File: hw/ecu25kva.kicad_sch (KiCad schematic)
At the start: 0 parts

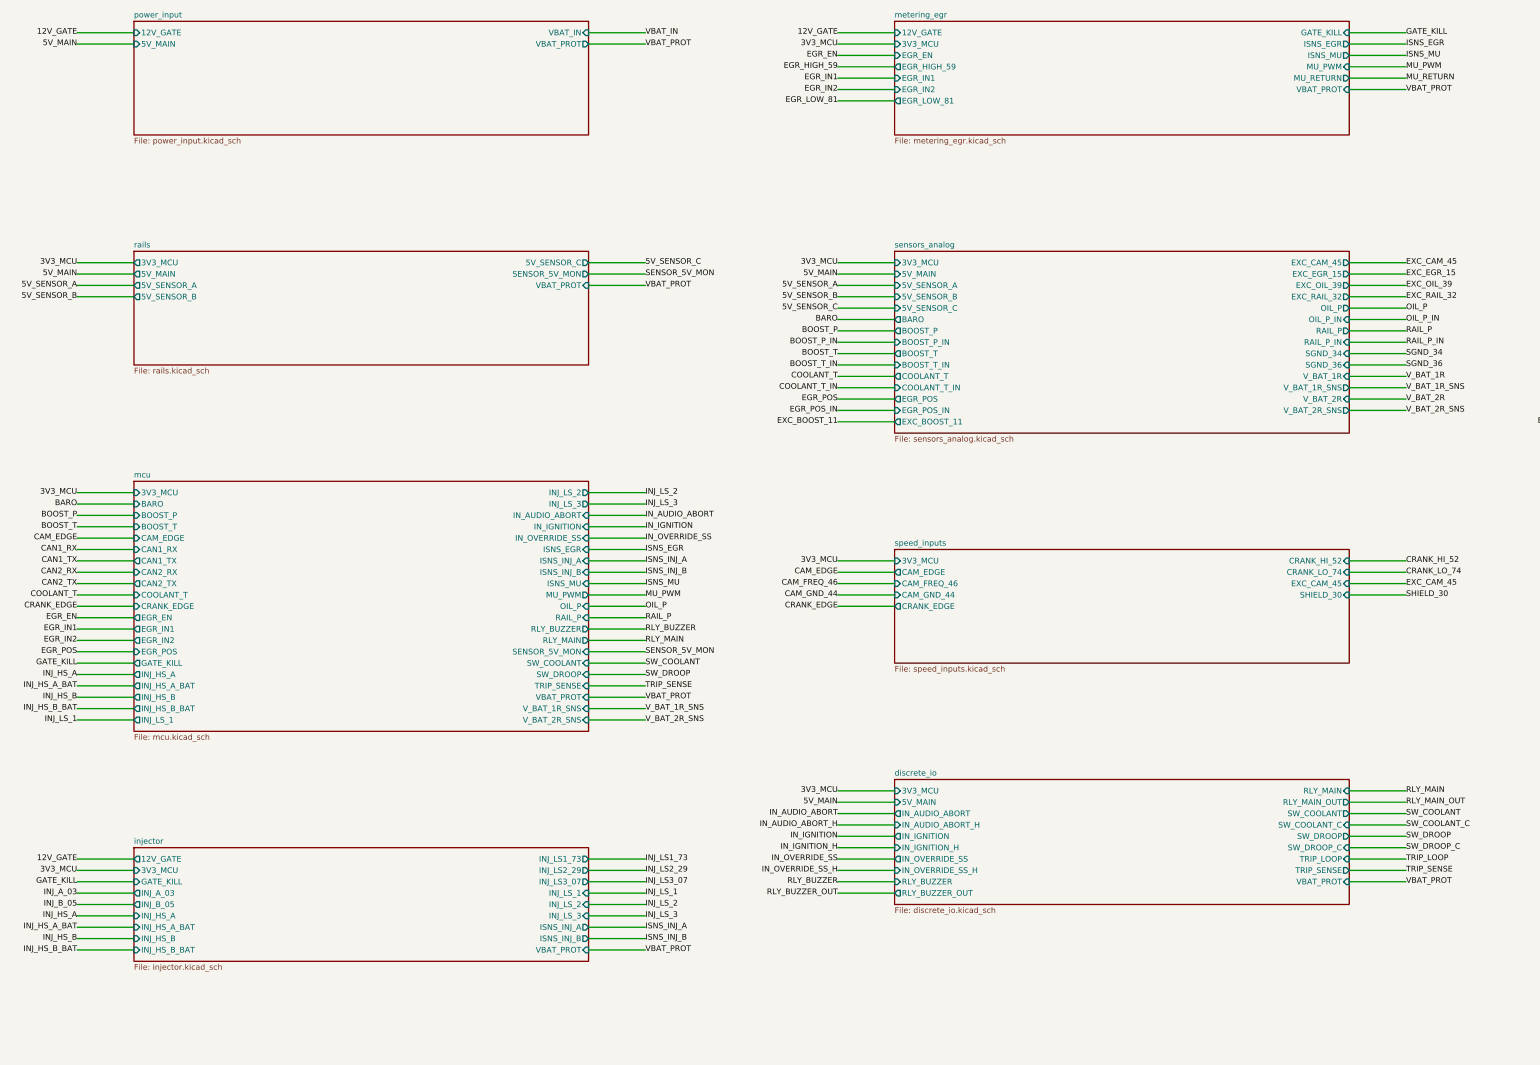
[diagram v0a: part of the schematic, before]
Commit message: Move the injector and EGR supply onto pins 04 and 06 (POWER-PATH)
Every high-current load drew through pin 21, whose reverse FET was
sized for 5 A and whose EMI filter never stated a DC current. Pin 04
now feeds VBAT_INJ (the injector hold switches and the boost power
stage), and pin 06 feeds VBAT_EGR (the EGR bridge). Each is fused 10 A
in the loom and has its own SMCJ43CA TVS, SQM120P10-10m1L reverse
P-FET (passive gate, as Q1), SS20PH102HM3 backstop and 2 x 2.2 uF.
Pin 21 keeps the buck, the relays, the metering freewheel and the
boost controller's VDD.

The pin-21 FET could not simply be copied: at the EGR's 6.4 A stall it
would pass its junction limit on a 105 C board. The new part, from
Vishay doc 76943 Rev. A, runs at Tj 139 C (155 C cranking) on the EGR
rail and 117 C on the injector rail. The new block power_path.cir
holds those figures as 18 checks. check_netlist now fails unless each
rail leaves its own FET for its own loads and VBAT_PROT reaches
neither power stage.

The sheets are generated against KiCad 7.0.11's symbol library, which
regenerates an unchanged sheet identically. KiCad 10's library would
have rewritten every embedded symbol.

Gates: 25/25 blocks; connectivity OK with the same 2 open items; 333
components, 314 with footprints; 208 passives packaged. The questions
put to the owner -- the split, the reverse protection, what stays on
pin 21, and the KiCad/ngspice choices -- are in decisions-log.md
sections 5 and 6. The spec, the BOM requirements, the handbook, status
and the handoff are updated to match, and the bible is rebuilt (333
pages).
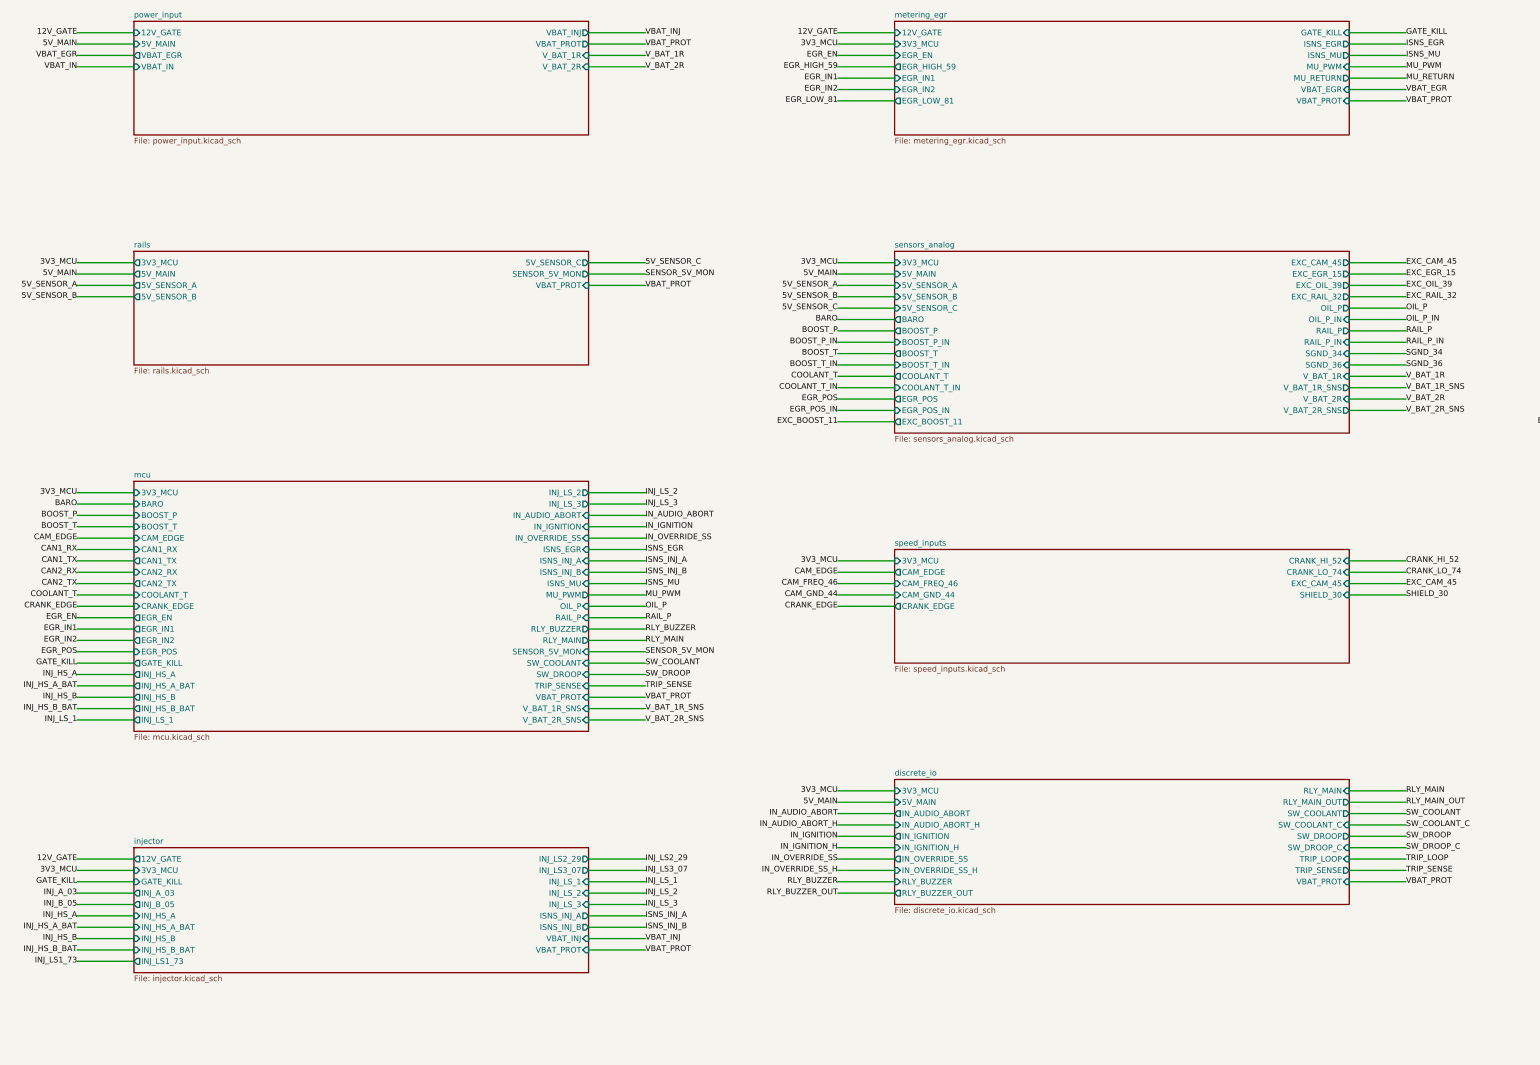
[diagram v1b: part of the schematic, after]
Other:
- sheet injector ports: added VBAT_INJ; removed none
- sheet metering_egr ports: added VBAT_EGR; removed none
- sheet power_input ports: added VBAT_EGR, VBAT_INJ, V_BAT_1R, V_BAT_2R; removed none
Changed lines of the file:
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@@
       (effects (font (size 1.27 1.27)) (justify left))
     )
-    (pin "VBAT_IN" input (at 146.60 30.54 0)
+    (pin "VBAT_EGR" output (at 45.00 35.62 180)
+      (effects (font (size 1.27 1.27)) (justify left))
+    )
+    (pin "VBAT_IN" input (at 45.00 38.16 180)
+      (effects (font (size 1.27 1.27)) (justify left))
+    )
+    (pin "VBAT_INJ" output (at 146.60 30.54 0)
       (effects (font (size 1.27 1.27)) (justify right))
     )
     (pin "VBAT_PROT" output (at 146.60 33.08 0)
+      (effects (font (size 1.27 1.27)) (justify right))
+    )
+    (pin "V_BAT_1R" input (at 146.60 35.62 0)
+      (effects (font (size 1.27 1.27)) (justify right))
+    )
+    (pin "V_BAT_2R" input (at 146.60 38.16 0)
       (effects (font (size 1.27 1.27)) (justify right))
     )
@@
     )
   )
-  (sheet (at 45.0 212.68) (size 101.6 25.40) (fields_autoplaced)
+  (sheet (at 45.0 212.68) (size 101.6 27.94) (fields_autoplaced)
     (stroke (width 0.1524) (type solid))
     (fill (color 0 0 0 0.0000))
@@
       (effects (font (size 1.27 1.27)) (justify left bottom))
     )
-    (property "Sheetfile" "injector.kicad_sch" (id 1) (at 45.0 238.64 0)
+    (property "Sheetfile" "injector.kicad_sch" (id 1) (at 45.0 241.18 0)
       (effects (font (size 1.27 1.27)) (justify left top))
     )
@@
       (effects (font (size 1.27 1.27)) (justify left))
     )
-    (pin "INJ_LS1_73" output (at 146.60 215.22 0)
-      (effects (font (size 1.27 1.27)) (justify right))
-    )
-    (pin "INJ_LS2_29" output (at 146.60 217.76 0)
-      (effects (font (size 1.27 1.27)) (justify right))
-    )
-    (pin "INJ_LS3_07" output (at 146.60 220.30 0)
-      (effects (font (size 1.27 1.27)) (justify right))
-    )
-    (pin "INJ_LS_1" input (at 146.60 222.84 0)
-      (effects (font (size 1.27 1.27)) (justify right))
-    )
-    (pin "INJ_LS_2" input (at 146.60 225.38 0)
-      (effects (font (size 1.27 1.27)) (justify right))
-    )
-    (pin "INJ_LS_3" input (at 146.60 227.92 0)
-      (effects (font (size 1.27 1.27)) (justify right))
-    )
-    (pin "ISNS_INJ_A" output (at 146.60 230.46 0)
-      (effects (font (size 1.27 1.27)) (justify right))
-    )
-    (pin "ISNS_INJ_B" output (at 146.60 233.00 0)
+    (pin "INJ_LS1_73" output (at 45.00 238.08 180)
+      (effects (font (size 1.27 1.27)) (justify left))
+    )
+    (pin "INJ_LS2_29" output (at 146.60 215.22 0)
+      (effects (font (size 1.27 1.27)) (justify right))
+    )
+    (pin "INJ_LS3_07" output (at 146.60 217.76 0)
+      (effects (font (size 1.27 1.27)) (justify right))
+    )
+    (pin "INJ_LS_1" input (at 146.60 220.30 0)
+      (effects (font (size 1.27 1.27)) (justify right))
+    )
+    (pin "INJ_LS_2" input (at 146.60 222.84 0)
+      (effects (font (size 1.27 1.27)) (justify right))
+    )
+    (pin "INJ_LS_3" input (at 146.60 225.38 0)
+      (effects (font (size 1.27 1.27)) (justify right))
+    )
+    (pin "ISNS_INJ_A" output (at 146.60 227.92 0)
+      (effects (font (size 1.27 1.27)) (justify right))
+    )
+    (pin "ISNS_INJ_B" output (at 146.60 230.46 0)
+      (effects (font (size 1.27 1.27)) (justify right))
+    )
+    (pin "VBAT_INJ" input (at 146.60 233.00 0)
       (effects (font (size 1.27 1.27)) (justify right))
     )
@@
       (effects (font (size 1.27 1.27)) (justify right))
     )
-    (pin "VBAT_PROT" input (at 316.60 43.24 0)
+    (pin "VBAT_EGR" input (at 316.60 43.24 0)
+      (effects (font (size 1.27 1.27)) (justify right))
+    )
+    (pin "VBAT_PROT" input (at 316.60 45.78 0)
       (effects (font (size 1.27 1.27)) (justify right))
     )
@@
     (effects (font (size 1.27 1.27)) (justify right))
   )
+  (wire (pts (xy 45.00 35.62) (xy 32.30 35.62))
+    (stroke (width 0) (type default))
+  )
+  (label "VBAT_EGR" (at 32.30 35.62 180)
+    (effects (font (size 1.27 1.27)) (justify right))
+  )
+  (wire (pts (xy 45.00 38.16) (xy 32.30 38.16))
+    (stroke (width 0) (type default))
+  )
+  (label "VBAT_IN" (at 32.30 38.16 180)
+    (effects (font (size 1.27 1.27)) (justify right))
+  )
   (wire (pts (xy 146.60 30.54) (xy 159.30 30.54))
     (stroke (width 0) (type default))
   )
-  (label "VBAT_IN" (at 159.30 30.54 0)
+  (label "VBAT_INJ" (at 159.30 30.54 0)
     (effects (font (size 1.27 1.27)) (justify left))
   )
@@
     (effects (font (size 1.27 1.27)) (justify left))
   )
+  (wire (pts (xy 146.60 35.62) (xy 159.30 35.62))
+    (stroke (width 0) (type default))
+  )
+  (label "V_BAT_1R" (at 159.30 35.62 0)
+    (effects (font (size 1.27 1.27)) (justify left))
+  )
+  (wire (pts (xy 146.60 38.16) (xy 159.30 38.16))
+    (stroke (width 0) (type default))
+  )
+  (label "V_BAT_2R" (at 159.30 38.16 0)
+    (effects (font (size 1.27 1.27)) (justify left))
+  )
   (wire (pts (xy 45.00 81.94) (xy 32.30 81.94))
     (stroke (width 0) (type default))
@@
     (effects (font (size 1.27 1.27)) (justify right))
   )
+  (wire (pts (xy 45.00 238.08) (xy 32.30 238.08))
+    (stroke (width 0) (type default))
+  )
+  (label "INJ_LS1_73" (at 32.30 238.08 180)
+    (effects (font (size 1.27 1.27)) (justify right))
+  )
   (wire (pts (xy 146.60 215.22) (xy 159.30 215.22))
     (stroke (width 0) (type default))
   )
-  (label "INJ_LS1_73" (at 159.30 215.22 0)
+  (label "INJ_LS2_29" (at 159.30 215.22 0)
     (effects (font (size 1.27 1.27)) (justify left))
   )
@@
     (stroke (width 0) (type default))
   )
-  (label "INJ_LS2_29" (at 159.30 217.76 0)
+  (label "INJ_LS3_07" (at 159.30 217.76 0)
     (effects (font (size 1.27 1.27)) (justify left))
   )
@@
     (stroke (width 0) (type default))
   )
-  (label "INJ_LS3_07" (at 159.30 220.30 0)
+  (label "INJ_LS_1" (at 159.30 220.30 0)
     (effects (font (size 1.27 1.27)) (justify left))
   )
@@
     (stroke (width 0) (type default))
   )
-  (label "INJ_LS_1" (at 159.30 222.84 0)
+  (label "INJ_LS_2" (at 159.30 222.84 0)
     (effects (font (size 1.27 1.27)) (justify left))
   )
@@
     (stroke (width 0) (type default))
   )
-  (label "INJ_LS_2" (at 159.30 225.38 0)
+  (label "INJ_LS_3" (at 159.30 225.38 0)
     (effects (font (size 1.27 1.27)) (justify left))
   )
@@
     (stroke (width 0) (type default))
   )
-  (label "INJ_LS_3" (at 159.30 227.92 0)
+  (label "ISNS_INJ_A" (at 159.30 227.92 0)
     (effects (font (size 1.27 1.27)) (justify left))
   )
@@
     (stroke (width 0) (type default))
   )
-  (label "ISNS_INJ_A" (at 159.30 230.46 0)
+  (label "ISNS_INJ_B" (at 159.30 230.46 0)
     (effects (font (size 1.27 1.27)) (justify left))
   )
@@
     (stroke (width 0) (type default))
   )
-  (label "ISNS_INJ_B" (at 159.30 233.00 0)
+  (label "VBAT_INJ" (at 159.30 233.00 0)
     (effects (font (size 1.27 1.27)) (justify left))
   )
@@
     (stroke (width 0) (type default))
   )
-  (label "VBAT_PROT" (at 329.30 43.24 0)
-    (effects (font (size 1.27 1.27)) (justify left))
-  )
+  (label "VBAT_EGR" (at 329.30 43.24 0)
+    (effects (font (size 1.27 1.27)) (justify left))
+  )
+  (wire (pts (xy 316.60 45.78) (xy 329.30 45.78))
+    (stroke (width 0) (type default))
+  )
+  (label "VBAT_PROT" (at 329.30 45.78 0)
+    (effects (font (size 1.27 1.27)) (justify left))
+  )
